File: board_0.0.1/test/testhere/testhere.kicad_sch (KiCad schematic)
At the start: 1 part, among them J1 TE_179686-6_104pin_Connector

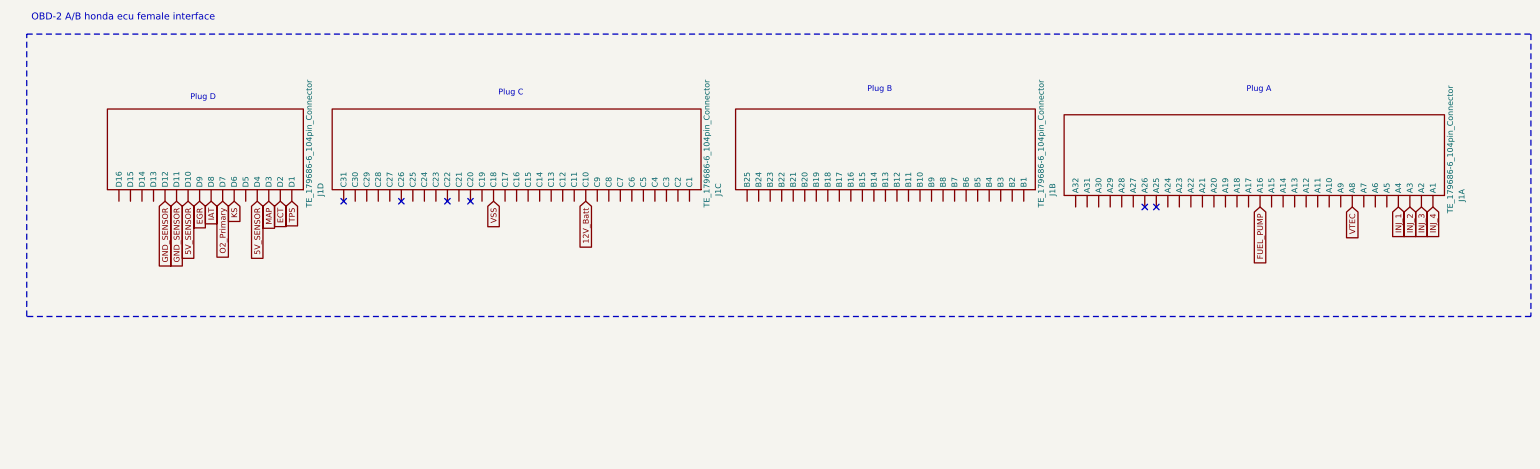
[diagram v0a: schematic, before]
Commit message: new VR conditioner that should work wis honda
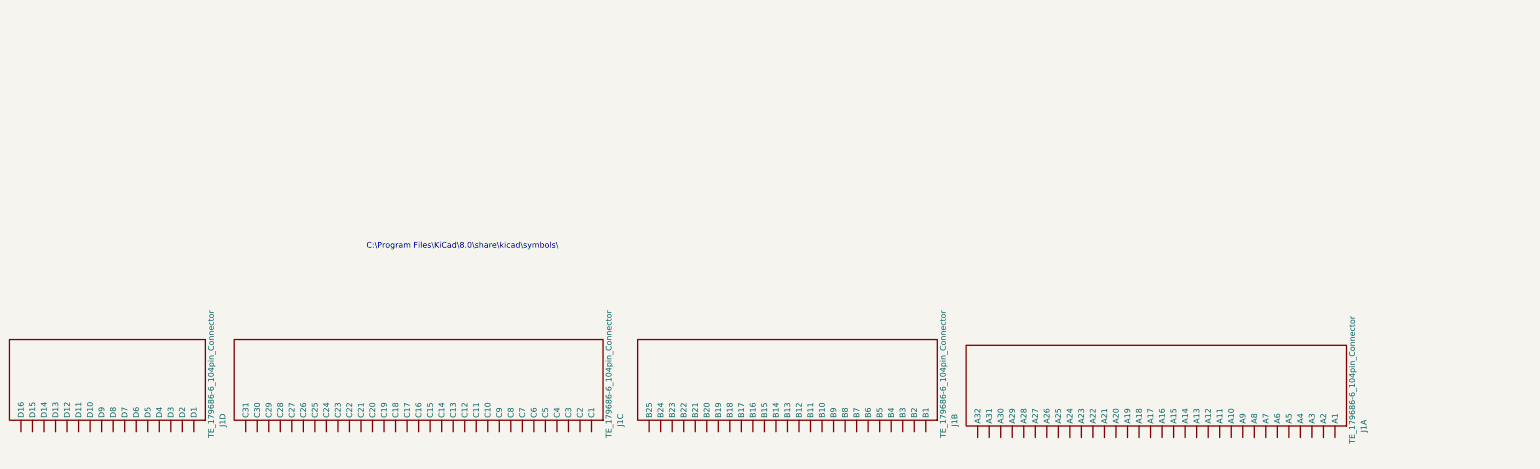
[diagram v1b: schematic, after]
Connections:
- net 12V_Batt: no longer names the net of J1.C10
- net 5V_SENSOR: no longer names the net of J1.D10
- net 5V_SENSOR: no longer J1.D4
- net ECT: no longer names the net of J1.D2
- net EGR: no longer names the net of J1.D9
- net FUEL_PUMP: no longer names the net of J1.A16
- net GND_SENSOR: no longer names the net of J1.D11
- net GND_SENSOR: no longer J1.D12
- net IAT: no longer names the net of J1.D8
- net INJ_1: no longer names the net of J1.A4
- net INJ_2: no longer names the net of J1.A3
- net INJ_3: no longer names the net of J1.A2
- net INJ_4: no longer names the net of J1.A1
- net KS: no longer names the net of J1.D6
- net MAP: no longer names the net of J1.D3
- net O2_Primary: no longer names the net of J1.D7
- net TPS: no longer names the net of J1.D1
- net VSS: no longer names the net of J1.C18
- net VTEC: no longer names the net of J1.A8
- no-connect marks 6 -> 0
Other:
- note added: "C:\Program Files\KiCad\8.0\share\kicad\symbols\"
- note removed: "OBD-2 A/B honda ecu female interface"
- note removed: "Plug A"
- note removed: "Plug B"
- note removed: "Plug C"
- note removed: "Plug D"
